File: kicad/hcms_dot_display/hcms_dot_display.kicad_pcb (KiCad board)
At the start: 2 copper layers, 35.5 x 39.9 mm, 40 parts, among them J1 Conn_01x11, J2 USB_C_Receptacle_USB2.0, J3 Conn_01x11, J4 Conn_01x10_Female, J5 Conn_01x10_Male, Q1 Q_PMOS_DSG, Q2 Q_PMOS_DSG, Q3 Q_PMOS_DSG, Q4 Q_PMOS_DSG, Q5 Q_PMOS_DSG, SW2 SW_SPST, U1 ATtiny824-SSF, U2 FT231XS

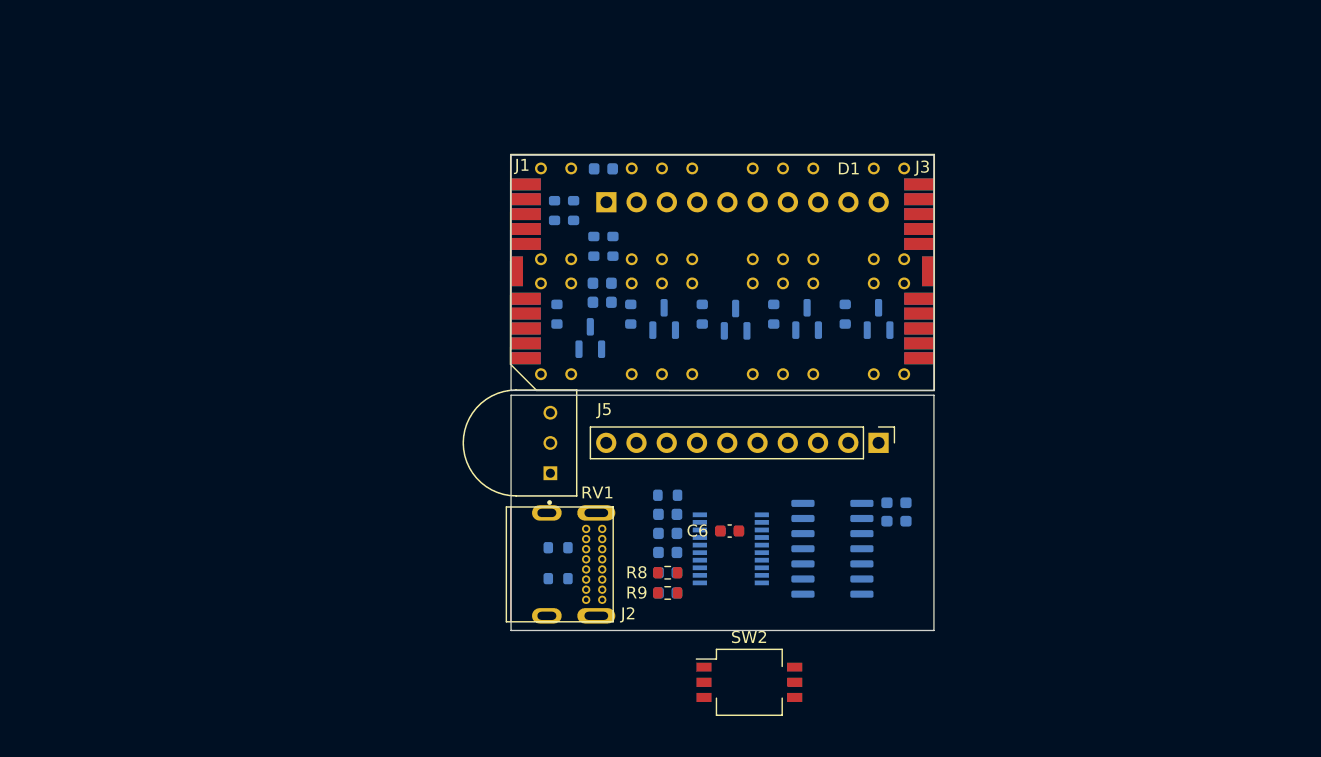
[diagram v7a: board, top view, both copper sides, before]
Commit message: Added Vcol rail and switching PMOS.  Started new board to board cons
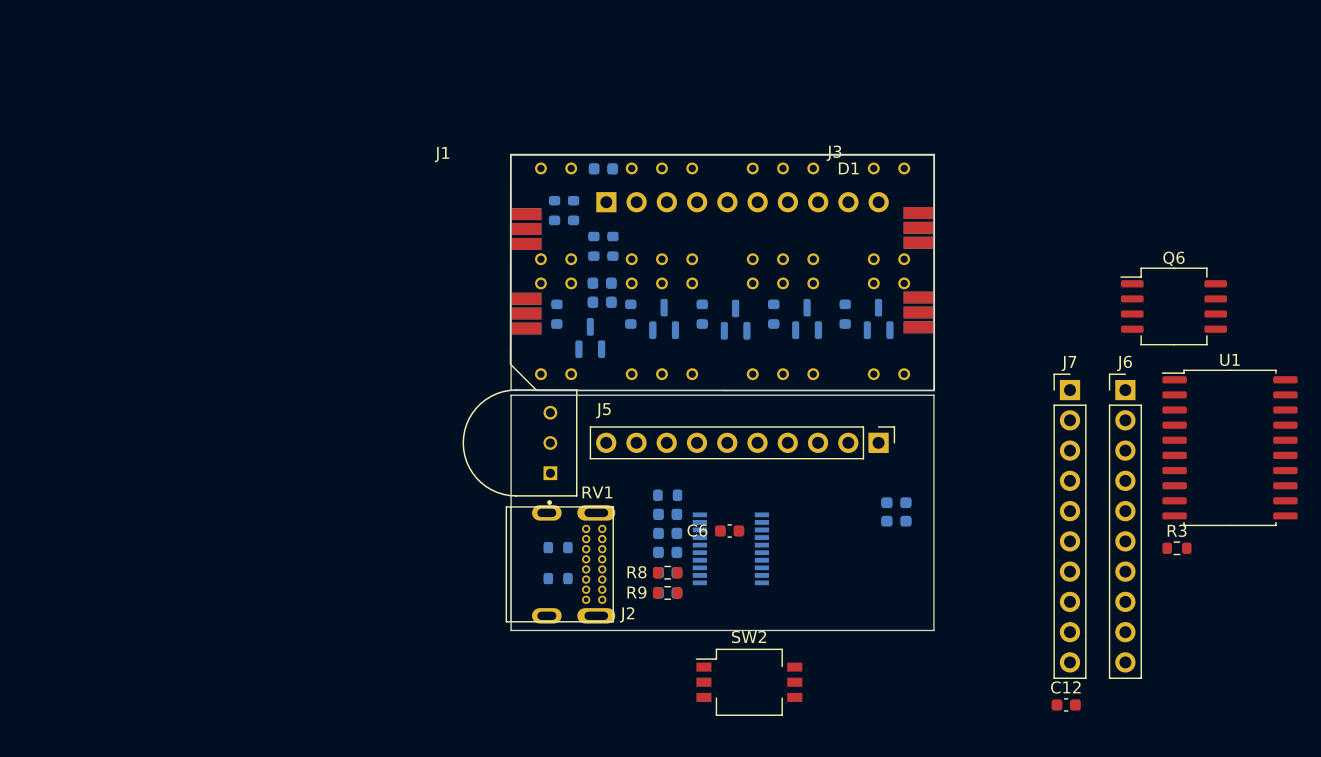
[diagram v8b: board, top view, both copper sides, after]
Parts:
- added C12: 100nF, Capacitor_SMD:C_0603_1608Metric, F.Cu at (209.3, 136.0)
- added J6: Conn_01x10_Male, Connector_PinHeader_2.54mm:PinHeader_1x10_P2.54mm_Vertical, F.Cu at (214.3, 109.6)
- added J7: Conn_01x10_Female, Connector_PinHeader_2.54mm:PinHeader_1x10_P2.54mm_Vertical, F.Cu at (209.7, 109.6)
- added Q6: Q_PMOS_DSG, Package_SO:SO-8_5.3x6.2mm_P1.27mm, F.Cu at (218.4, 102.5)
- added R3: 200, Resistor_SMD:R_0603_1608Metric, F.Cu at (218.7, 122.8)
- J1: value Conn_01x11 -> Conn_01x12; footprint hcms:input board to board con -> hcms:input board to board con top bot
- J3: value Conn_01x11 -> Conn_01x12; footprint hcms:output board to board con -> hcms:input board to board con top bot
- U1: value ATtiny824-SSF -> ATtiny826-SXX; footprint Package_SO:SOIC-14_3.9x8.7mm_P1.27mm -> Package_SO:SOIC-20W_7.5x12.8mm_P1.27mm; moved to F.Cu
- moved U1 34.4 mm to (223.1, 114.4), turned to 0 degrees
- moved J1 0.07 mm to (164.1, 99.7)
- moved J3 0.07 mm to (196.9, 99.5)
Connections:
- J1 pad 10: /DAISY_B_DATA -> /DAISY_A_DATA
- J1 pad 11: GND -> /DAISY_B_DATA
- J1 pad 2: /MCU_COL_1 -> /V_COL
- J1 pad 3: /MCU_COL_2 -> /MCU_COL_1
- J1 pad 4: /MCU_COL_3 -> /MCU_COL_2
- J1 pad 5: /MCU_COL_4 -> /MCU_COL_3
- J1 pad 6: /MCU_COL_5 -> /MCU_COL_4
- J1 pad 7: /nBLNK -> /MCU_COL_5
- J1 pad 8: /CLK -> /nBLNK
- J1 pad 9: /DAISY_A_DATA -> /CLK
- J3 pad 10: /B_DATA -> /DAISY_A_DATA
- J3 pad 11: GND -> /DAISY_B_DATA
- J3 pad 2: /MCU_COL_1 -> /V_COL
- J3 pad 3: /MCU_COL_2 -> /MCU_COL_1
- J3 pad 4: /MCU_COL_3 -> /MCU_COL_2
- J3 pad 5: /MCU_COL_4 -> /MCU_COL_3
- J3 pad 6: /MCU_COL_5 -> /MCU_COL_4
- J3 pad 7: /nBLNK -> /MCU_COL_5
- J3 pad 8: /CLK -> /nBLNK
- J3 pad 9: /A_DATA -> /CLK
- Q1 pad 2: +5V -> /V_COL
- Q2 pad 2: +5V -> /V_COL
- Q3 pad 2: +5V -> /V_COL
- Q4 pad 2: +5V -> /V_COL
- Q5 pad 2: +5V -> /V_COL
- U1 pad 10: /MCU_COL_3 -> /MCU_COL_2
- U1 pad 11: /MCU_COL_2 -> /MCU_COL_1
- U1 pad 12: /MCU_COL_1 -> unconnected-(U1-Pad12)
- U1 pad 13: /UPDI -> unconnected-(U1-Pad13)
- U1 pad 14: GND -> unconnected-(U1-Pad14)
- U1 pad 2: /MCU_DATA -> unconnected-(U1-Pad2)
- U1 pad 3: unconnected-(U1-Pad3) -> /CLK
- U1 pad 4: /nBLNK -> unconnected-(U1-Pad4)
- U1 pad 5: unconnected-(U1-Pad5) -> /nBLNK
- U1 pad 6: /POT -> /MCU_DATA
- U1 pad 7: /CLK -> /MCU_COL_5
- U1 pad 8: /MCU_COL_5 -> /MCU_COL_4
- U1 pad 9: /MCU_COL_4 -> /MCU_COL_3
